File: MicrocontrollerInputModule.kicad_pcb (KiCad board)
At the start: 2 copper layers, 33.8 x 131 mm, 47 parts, among them J1 Conn_02x04_Odd_Even, J2 Conn_01x16, J3 Conn_01x10, SW1 KXT3, SW2 KXT3, U1 W25Q16JVUXIQ, U2 RP2040, Y1 12.000MHz

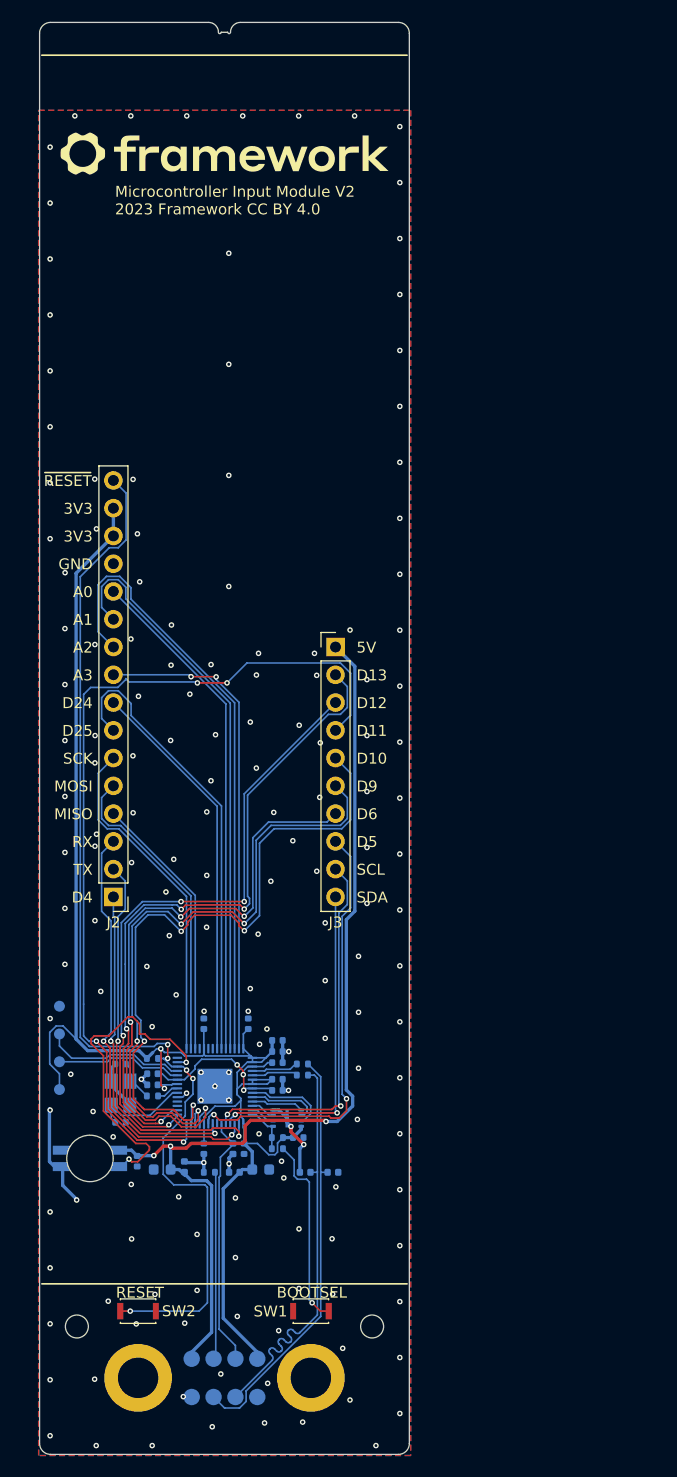
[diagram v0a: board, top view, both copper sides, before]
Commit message: Initial reconfiguration for X1 Carbon Gen10 Keyboard module
RP2040 pin assignments are somewhat arbitrary; PCB is not yet routed;
position of framework input module connector is also arbitrary.
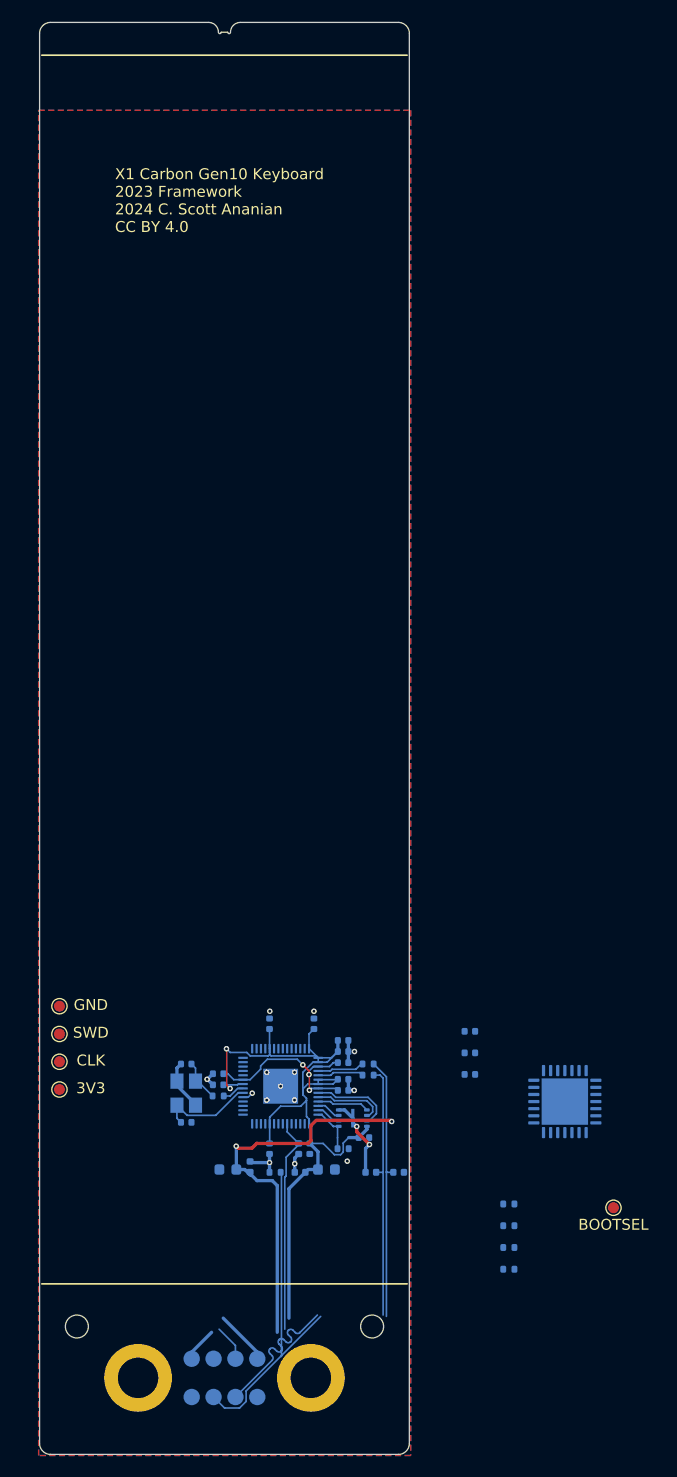
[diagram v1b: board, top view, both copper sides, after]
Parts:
- removed D6: SK6812MINI-E, InputModule:LED_SK6812MINI-E_PLCC4_3.5x3.5mm_P1.75mm
- removed G***: LOGO, InputModule:Framework-Logo_3.8mm_SilkScreen
- removed J2: Conn_01x16, Connector_PinHeader_2.54mm:PinHeader_1x16_P2.54mm_Vertical
- removed J3: Conn_01x10, Connector_PinHeader_2.54mm:PinHeader_1x10_P2.54mm_Vertical
- removed R2: 10k, Resistor_SMD:R_0402_1005Metric
- removed SW1, SW2: KXT3, Button_Switch_SMD:SW_SPST_CK_KXT3
- added C18: 100nF, Capacitor_SMD:C_0402_1005Metric, B.Cu at (89.4, 144.3)
- added C19: 47uF, Capacitor_SMD:C_0402_1005Metric, B.Cu at (89.4, 146.2)
- added R10: 100, Resistor_SMD:R_0402_1005Metric, B.Cu at (92.9, 164.1)
- added R8: 100, Resistor_SMD:R_0402_1005Metric, B.Cu at (92.9, 160.1)
- added R9: 100, Resistor_SMD:R_0402_1005Metric, B.Cu at (92.9, 162.1)
- added TP5: BOOTSEL, TestPoint:TestPoint_Pad_D1.0mm, F.Cu at (102.5, 158.4)
- added U4: MCP23017_ML, Package_DFN_QFN:QFN-28-1EP_6x6mm_P0.65mm_EP4.25x4.25mm, B.Cu at (98.0, 148.7)
- R4: value 10k -> 100
- TP1: value TestPoint -> 3V3; moved to F.Cu
- TP2: value TestPoint -> CLK; moved to F.Cu
- TP3: value TestPoint -> SWD; moved to F.Cu
- TP4: value TestPoint -> GND; moved to F.Cu
- moved R4 35.2 mm to (92.9, 158.1), turned to 180 degrees
- moved C17 32.7 mm to (89.4, 142.3), turned to 180 degrees
- moved C10 6.01 mm to (74.7, 153.0)
- moved C11 6.01 mm to (75.1, 141.6)
- moved C12 6.01 mm to (71.0, 153.0)
- moved C13 6.01 mm to (71.0, 141.6)
- moved C15 6.01 mm to (67.2, 154.9)
- moved C16 6.01 mm to (76.2, 154.9)
- moved C3 6.01 mm to (79.7, 152.0)
- moved C5 6.01 mm to (77.8, 147.7)
- moved C6 6.01 mm to (77.8, 145.2)
- moved C7 6.01 mm to (77.8, 144.1)
- moved C8 6.01 mm to (77.8, 143.1)
- moved C9 6.01 mm to (77.8, 146.7)
- moved D1 6.01 mm to (73.8, 155.2)
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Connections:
- C17 pad 1: +5V -> GND
- C17 pad 2: GND -> +3V3
- R1 pad 1: Net-(R1-Pad1) -> /~{HOTKEY}
- R4 pad 1: +3V3 -> /~{LED_FNLOCK}
- R4 pad 2: /~{RESET} -> /~{LED_FNLOCK_R}
- U2 pad 11: /D6 -> /IOEXP_SDA
- U2 pad 12: /D9 -> /IOEXP_SCK
- U2 pad 13: /D10 -> /IOEXP_INT
- U2 pad 14: /D11 -> /~{IOEXP_RESET}
- U2 pad 15: /D12 -> /~{LED_FNLOCK}
- U2 pad 16: /D13 -> /~{LED_MUTE}
- U2 pad 17: unconnected-(U2-GPIO14-Pad17) -> /~{LED_MICMUTE}
- U2 pad 18: unconnected-(U2-GPIO15-Pad18) -> /~{LED_CAPSLOCK}
- U2 pad 2: /TX -> /SENSE0
- U2 pad 26: /~{RESET} -> unconnected-(U2-RUN-Pad26)
- U2 pad 27: /LED -> /~{HOTKEY}
- U2 pad 28: unconnected-(U2-GPIO17-Pad28) -> /TP4DATA
- U2 pad 29: /SCK -> /TP4RESET
- U2 pad 3: /RX -> /SENSE1
- U2 pad 30: /MOSI -> /TP4CLK
- U2 pad 31: /MISO -> /~{TP4ACT}
- U2 pad 32: unconnected-(U2-GPIO21-Pad32) -> /~{TP4_FW_WR_EN}
- U2 pad 34: unconnected-(U2-GPIO22-Pad34) -> /KBD_BL_PWM
- U2 pad 35: unconnected-(U2-GPIO23-Pad35) -> /~{KBD_BL_DET}
- U2 pad 36: /D24 -> /~{SLEEP}
- U2 pad 37: /D25 -> unconnected-(U2-GPIO25-Pad37)
- U2 pad 38: /A0 -> unconnected-(U2-GPIO26_ADC0-Pad38)
- U2 pad 39: /A1 -> unconnected-(U2-GPIO27_ADC1-Pad39)
- U2 pad 4: /SDA -> /SENSE2
- U2 pad 40: /A2 -> unconnected-(U2-GPIO28_ADC2-Pad40)
- U2 pad 41: /A3 -> unconnected-(U2-GPIO29_ADC3-Pad41)
- U2 pad 5: /SCL -> /SENSE3
- U2 pad 6: /~{SLEEP} -> /SENSE4
- U2 pad 7: unconnected-(U2-GPIO5-Pad7) -> /SENSE5
- U2 pad 8: /D4 -> /SENSE6
- U2 pad 9: /D5 -> /SENSE7
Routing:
- net /~{RESET}: track 101.1 -> 0.00 mm, vias 5 -> 0
- net /D11: track 81.5 -> 0.00 mm, vias 4 -> 0
- net +3V3: track 145.5 -> 77.9 mm
- net /D10: track 62.3 -> 0.00 mm, vias 4 -> 0
- net /D13: track 61.6 -> 0.00 mm, vias 4 -> 0
- net /D9: track 58.9 -> 0.00 mm, vias 4 -> 0
- net /D12: track 57.1 -> 0.00 mm, vias 4 -> 0
- net /A2: track 56.1 -> 0.00 mm
- net /D6: track 55.9 -> 0.00 mm, vias 4 -> 0
- net /A1: track 52.4 -> 0.00 mm
- net +5V: track 91.0 -> 39.3 mm, vias 3 -> 2
- net /A0: track 46.1 -> 0.00 mm
- net /A3: track 44.4 -> 0.00 mm, vias 2 -> 0
- net /D25: track 41.9 -> 0.00 mm
- net /D5: track 39.8 -> 0.00 mm, vias 2 -> 0
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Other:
- board text added: "X1 Carbon Gen10 Keyboard 2023 Framework 2024 C. Scott Ananian CC BY 4.0"
- board text removed: "3V3"
- board text removed: "5V"
- board text removed: "A0"
- board text removed: "A1"
- board text removed: "A2"
- board text removed: "A3"
- board text removed: "BOOTSEL"
- board text removed: "CLK"
- board text removed: "D10"
- board text removed: "D11"
- board text removed: "D12"
- board text removed: "D13"
- board text removed: "D24"
- board text removed: "D25"
- board text removed: "D4"
- board text removed: "D5"
- board text removed: "D6"
- board text removed: "D9"
- board text removed: "GND"
- board text removed: "MISO"
- board text removed: "MOSI"
- board text removed: "Microcontroller Input Module V2 2023 Framework CC BY 4.0"
- board text removed: "RESET"
- board text removed: "RX"
- board text removed: "SCK"
- board text removed: "SCL"
- board text removed: "SDA"
- board text removed: "SWD"
- board text removed: "TX"
- board text removed: "~{RESET}"

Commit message: First complete version, fully routed
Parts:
- added C20: 100nF, Capacitor_SMD:C_0402_1005Metric, B.Cu at (60.7, 153.2)
- added J3: IPEX 20655-045E-01, 20655-045E-01:IPEX_20655-045E-01, B.Cu at (58.8, 141.1)
- moved U4 42.2 mm to (56.0, 152.1)
- moved C19 38.1 mm to (51.3, 145.7), turned to 0 degrees
- moved TP4 31.2 mm to (82.0, 147.8), turned to 180 degrees
- moved R4 31.2 mm to (62.0, 154.3), turned to 90 degrees
- moved TP1 31.1 mm to (82.0, 140.2), turned to 180 degrees
- moved R9 30.5 mm to (63.4, 154.3), turned to 90 degrees
- moved TP3 30.3 mm to (82.0, 145.2), turned to 180 degrees
- moved TP2 30.3 mm to (82.0, 142.7), turned to 180 degrees
- moved R10 29.7 mm to (64.9, 154.3), turned to 90 degrees
- moved C18 28.6 mm to (61.0, 147.9), turned to -90 degrees
- moved R8 28.6 mm to (66.3, 149.7)
- moved TP5 21.3 mm to (82.0, 152.6), turned to 180 degrees
- moved C17 21.0 mm to (68.4, 141.0), turned to -90 degrees
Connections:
- U2 pad 11: /IOEXP_SDA -> /~{LED_CAPSLOCK}
- U2 pad 12: /IOEXP_SCK -> /~{LED_MICMUTE}
- U2 pad 13: /IOEXP_INT -> /~{LED_FNLOCK}
- U2 pad 14: /~{IOEXP_RESET} -> /KBD_BL_PWM
- U2 pad 15: /~{LED_FNLOCK} -> /~{TP4ACT}
- U2 pad 16: /~{LED_MUTE} -> /TP4RESET
- U2 pad 17: /~{LED_MICMUTE} -> /~{HOTKEY}
- U2 pad 18: /~{LED_CAPSLOCK} -> /~{LED_MUTE}
- U2 pad 2: /SENSE0 -> /IOEXP_SDA
- U2 pad 27: /~{HOTKEY} -> /SENSE5
- U2 pad 28: /TP4DATA -> /SENSE0
- U2 pad 29: /TP4RESET -> /SENSE2
- U2 pad 3: /SENSE1 -> /IOEXP_SCK
- U2 pad 30: /TP4CLK -> /SENSE1
- U2 pad 31: /~{TP4ACT} -> /SENSE7
- U2 pad 32: /~{TP4_FW_WR_EN} -> /SENSE4
- U2 pad 34: /KBD_BL_PWM -> /SENSE3
- U2 pad 35: /~{KBD_BL_DET} -> /SENSE6
- U2 pad 36: /~{SLEEP} -> /~{KBD_BL_DET}
- U2 pad 4: /SENSE2 -> /~{IOEXP_RESET}
- U2 pad 5: /SENSE3 -> /IOEXP_INT
- U2 pad 6: /SENSE4 -> /~{SLEEP}
- U2 pad 7: /SENSE5 -> /~{TP4_FW_WR_EN}
- U2 pad 8: /SENSE6 -> /TP4CLK
- U2 pad 9: /SENSE7 -> /TP4DATA
- U4 pad 1: /DRV12 -> /DRV2
- U4 pad 17: /DRV0 -> /DRV11
- U4 pad 18: /DRV1 -> /DRV8
- U4 pad 19: /DRV2 -> /DRV10
- U4 pad 2: /DRV13 -> /DRV4
- U4 pad 20: /DRV3 -> /DRV12
- U4 pad 21: /DRV4 -> /DRV9
- U4 pad 22: /DRV5 -> /DRV13
- U4 pad 23: /DRV6 -> /DRV15
- U4 pad 24: /DRV7 -> /DRV5
- U4 pad 25: /DRV8 -> /DRV7
- U4 pad 26: /DRV9 -> /DRV6
- U4 pad 27: /DRV10 -> /DRV3
- U4 pad 28: /DRV11 -> /DRV1
- U4 pad 3: /DRV14 -> /DRV0
- U4 pad 4: /DRV15 -> /DRV14
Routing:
- net GND: track 23.3 -> 128.7 mm, vias 16 -> 36
- net +3V3: track 77.9 -> 147.6 mm, vias 2 -> 9
- net /~{HOTKEY}: track 0.00 -> 42.9 mm, vias 0 -> 3
- net /~{TP4_FW_WR_EN}: track 0.00 -> 34.6 mm, vias 0 -> 2
- net /TP4CLK: track 0.00 -> 33.4 mm, vias 0 -> 2
- net /TP4DATA: track 0.00 -> 32.2 mm, vias 0 -> 2
- net /KBD_BL_PWM: track 0.00 -> 28.7 mm, vias 0 -> 2
- net /IOEXP_INT: track 0.00 -> 27.4 mm, vias 0 -> 2
- net /~{KBD_BL_DET}: track 0.00 -> 27.1 mm, vias 0 -> 2
- net /~{TP4ACT}: track 0.00 -> 26.8 mm, vias 0 -> 2
- net /~{IOEXP_RESET}: track 0.00 -> 26.2 mm, vias 0 -> 2
- net /IOEXP_SDA: track 0.00 -> 26.1 mm, vias 0 -> 2
- net /TP4RESET: track 0.00 -> 25.7 mm, vias 0 -> 2
- net /~{LED_CAPSLOCK_R}: track 0.00 -> 23.3 mm, vias 0 -> 2
- net /IOEXP_SCK: track 0.00 -> 22.6 mm, vias 0 -> 2
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
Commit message: Renumber components, tidy up silkscreen
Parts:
- renumbered C3 to C1, C8 to C10, C9 to C11, C10 to C12, C11 to C13, C12 to C14, C20 to C15, C13 to C16, C14 to C17, C1 to C2, C17 to C20, C2 to C3, C15 to C5, C5 to C6, C6 to C7, C16 to C8, C7 to C9, J3 to J2, R7 to R2, R5 to R4, R6 to R5, R4 to R6, R8 to R7, R9 to R8, R10 to R9, TP5 to TP1, TP1 to TP2, TP2 to TP3, TP3 to TP4, TP4 to TP5, U4 to U3
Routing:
- net GND: track 128.7 -> 139.4 mm

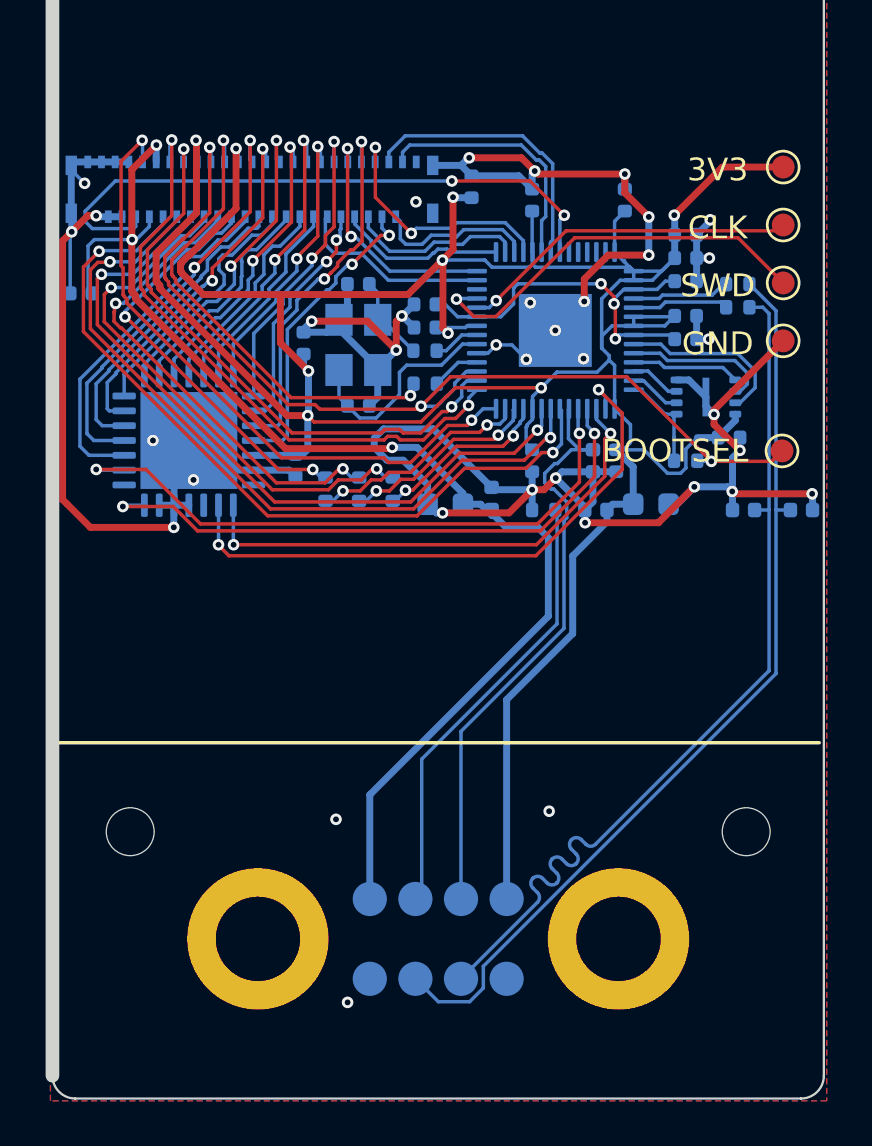
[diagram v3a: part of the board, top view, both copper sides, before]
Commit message: Update README; change C19 to an 0603 cap; improve ground plane connectivity
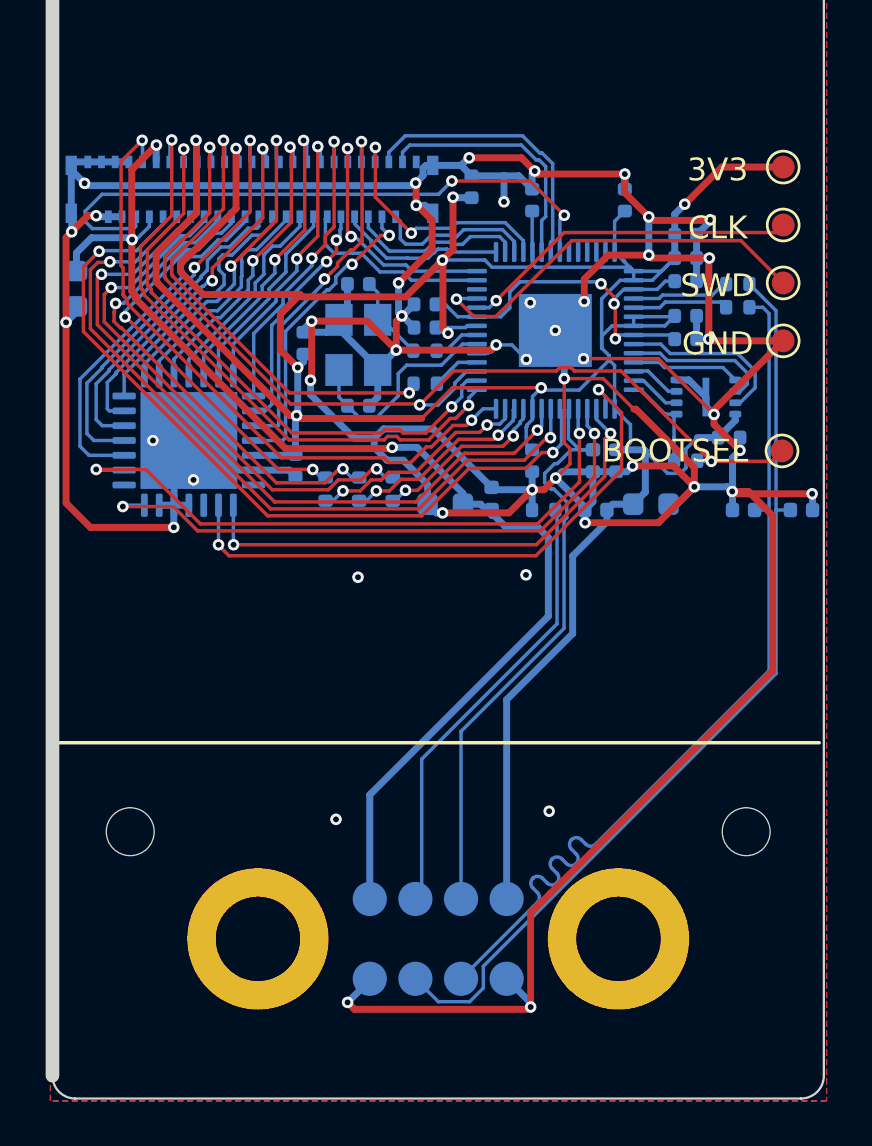
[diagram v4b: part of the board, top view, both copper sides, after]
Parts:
- C19: footprint Capacitor_SMD:C_0402_1005Metric -> Capacitor_SMD:C_0603_1608Metric
- moved C19 0.29 mm to (51.1, 145.5), turned to 90 degrees
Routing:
- net GND: track 139.4 -> 251.1 mm, vias 36 -> 46
- net +5V: track 55.5 -> 54.8 mm

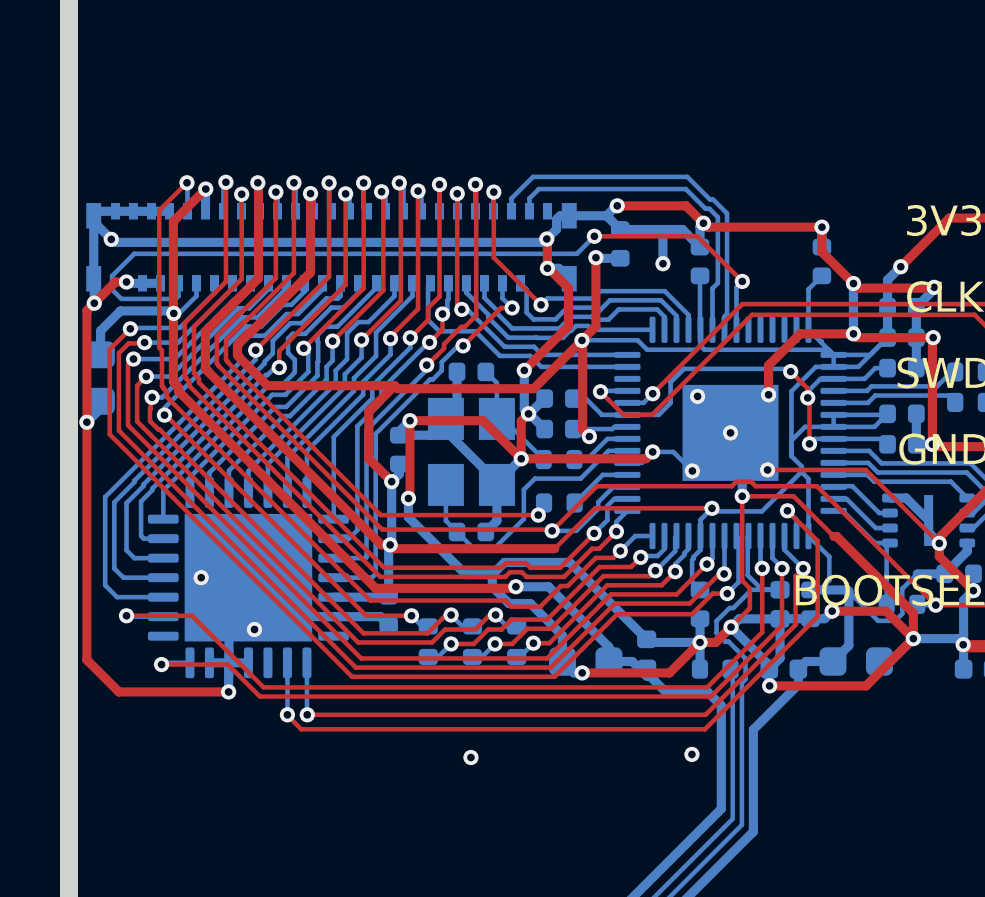
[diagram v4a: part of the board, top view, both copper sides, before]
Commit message: Swap TP4CLK and TP4DATA to handle PIO requirements
The current RP2040 PS/2 driver in:

https://github.com/qmk/qmk_firmware/blob/master/platforms/chibios/drivers/vendor/RP/RP2040/ps2_vendor.c#L24

requires that PS2_DATA_PIN is the one *before* PS2_CLOCK_PIN, so swap our
GPIO assignments to match.
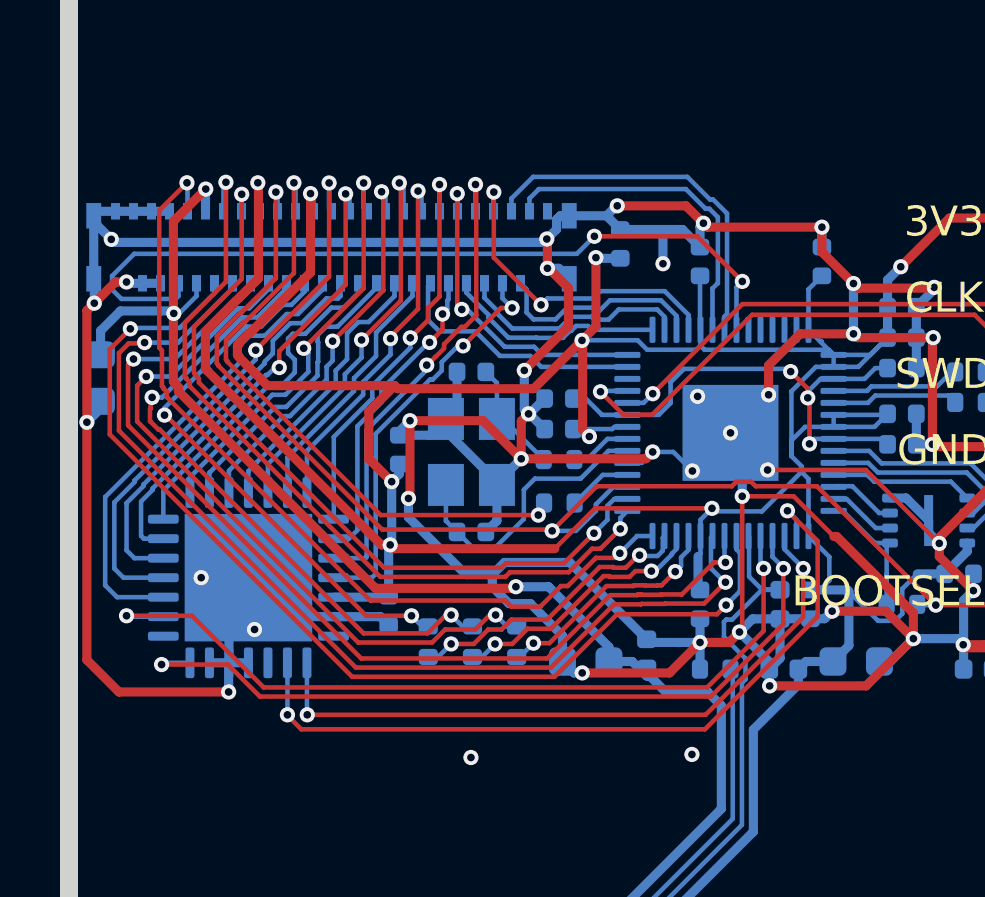
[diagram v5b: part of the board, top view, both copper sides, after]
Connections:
- U2 pad 8: /TP4CLK -> /TP4DATA
- U2 pad 9: /TP4DATA -> /TP4CLK
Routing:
- net /TP4DATA: track 32.2 -> 32.7 mm
